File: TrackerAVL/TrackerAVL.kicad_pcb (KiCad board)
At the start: 2 copper layers, 120 x 80 mm, 173 parts, among them J801 Conn_02x07_Odd_Even, J802 Conn_01x15, J803 Conn_01x04, P201 uC_debug, Q201 DTC043ZEBTL, Q202 DTC043ZEBTL, Q203 DTC043ZEBTL, Q701 2N7002P, Q702 2N7002P, Q703 2N7002P, Q704 DTC043ZEBTL, U201 MAX3221, U202 LPC4337JBD144, U203 STS8C5H30L, U301 MPU-6050, U401 NAU8814, U501 STS8C5H30L, U502 LD1085D2T33R, U503 NCP114ASN180T1G, U601 MPCIE-Socket, U701 74LVC244APW, U801 74HC4053, X201 12MHz, X202 32.768K

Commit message: Cambios en pcb
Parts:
- moved JP203 3.41 mm to (210.4, 131.7)
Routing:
- net +3V3: track 450.8 -> 592.7 mm, vias 63 -> 76
- net /CPU/U2_RXD: track 0.00 -> 135.5 mm, vias 0 -> 4
- net /CPU/U2_TXD: track 0.00 -> 134.4 mm, vias 0 -> 4
- net /MIC+: track 22.7 -> 139.7 mm, vias 0 -> 4
- net /MIC-: track 17.8 -> 128.3 mm, vias 0 -> 4
- net GNDS: track 41.8 -> 144.7 mm, vias 3 -> 7
- net /CPU/SLEEP_MDM: track 0.00 -> 97.7 mm, vias 0 -> 2
- net /CPU/DIG_OUT_0: track 6.49 -> 87.4 mm, vias 0 -> 4
- net /CPU/IGN: track 0.00 -> 79.5 mm, vias 0 -> 12
- net /CPU/DIG_OUT_1: track 9.93 -> 85.5 mm, vias 0 -> 4
- net /CPU/U3_RX: track 37.3 -> 111.3 mm, vias 4 -> 2
- net /VBAT: track 32.4 -> 102.5 mm, vias 0 -> 6
- net /CPU/DIG_OUT_2: track 13.5 -> 83.7 mm, vias 0 -> 4
- net /CPU/U3_TX: track 39.0 -> 107.9 mm
- net /CPU/BUZZER: track 19.1 -> 84.2 mm, vias 0 -> 6
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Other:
- net class Default: clearance 0.25 -> 0.2
- rule trace_clearance: 0.25 -> 0.2

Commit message: PCB terminado, pendiente revisión
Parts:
- moved F103 83.0 mm to (124.0, 60.8)
- moved F104 75.8 mm to (206.5, 133.2)
- moved FB502 13.1 mm to (163.9, 115.8)
- moved R501 13.1 mm to (134.9, 124.7)
- moved U501 13.1 mm to (140.6, 123.8)
- moved C302 13.1 mm to (153.4, 59.6)
- moved C201 13.1 mm to (130.4, 126.2)
- moved C202 13.1 mm to (173.7, 99.1)
- moved C203 13.1 mm to (171.5, 99.1)
- moved C204 13.1 mm to (122.5, 133.0)
- moved C205 13.1 mm to (124.5, 133.0)
- moved C206 13.1 mm to (150.8, 72.9)
- moved C207 13.1 mm to (124.5, 129.0)
- moved C208 13.1 mm to (158.5, 76.8)
- moved C209 13.1 mm to (158.5, 79.3)
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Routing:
- net GNDS: track 144.7 -> 146.4 mm
- net GND: track 488.6 -> 487.1 mm
- net (no net): track 0.76 -> 0.00 mm
- added copper zone on B.Cu, net (none)
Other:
- board text added: "Equipo AVL vRaptor v1.0 STA"
- board text added: "Industria Argentina"
- board text added: "Referencia: Mayer (Tecnología 8 mils) Pistas: 1.5; 1; 0.75; 0.5; 0.25; 0.20 [mm] Vías: 0.8 - Agujero: 0.4 [mm] Márgen: 0.25 mm Pista más delgada: 0.2 mm Dist. a borde: 0.3 mm STACK-UP FR4 1.6 mm Dual layer Componentes en capa superior Máscara anti-soldante: Azul Sin requerimientos especiales Terminación: HASL c/Pb Espesor de Cu: 1oz"
- board text added: "[ 2]"
- board text added: "[1 ]"
- board text removed: "Equipo AVL vRaptor v1.0 Referencia: Mayer (Tecnología 8 mils) Pistas: 1,5; 1; 0,75; 0,5; 0,25 [mm] Vía: 1mm - Agujero: 0,5mm Márgen: 0,25mm Pista más delgada: 0,25mm Dist. a borde: 0,3mm STACK-UP FR4 1,6mm Dual layer Componentes en capa superior Máscara anti-soldante: Azul Sin requerimientos especiales Terminación: HASL c/Pb Espesor de Cu: 1oz"
- board text removed: "Recomendaciones diseño > Cruces de pista entre capas a 90° > Colocar buenos planos de masa > Considerar poner vías térmicas > Uniones entre pads y pistas "teardrop" > Para plano de masa, clearance 0.25mm mínimo > Colocar jumpers-open para medir consumos > Orientación silkscreen "para un mismo lado""

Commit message: PCB terminado, pendiente revisión
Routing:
- net +3V3: track 592.7 -> 620.1 mm, vias 76 -> 78
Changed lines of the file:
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@@
     (thickness 1.6)
     (drawings 32)
-    (tracks 2622)
+    (tracks 2634)
     (zones 0)
     (modules 173)
@@
   )
   (setup
-    (last_trace_width 0.5)
+    (last_trace_width 0.75)
     (user_trace_width 0.2)
     (user_trace_width 0.24)
@@
   (segment (start 125.95 68.95) (end 130.123008 73.123008) (width 0.5) (layer B.Cu) (net 2))
   (segment (start 138.45 80.5) (end 131.5 73.55) (width 0.5) (layer F.Cu) (net 2))
-  (segment (start 146.850001 107.350001) (end 163.950001 107.350001) (width 1.5) (layer F.Cu) (net 2))
   (segment (start 146 106.5) (end 146.850001 107.350001) (width 1.5) (layer F.Cu) (net 2))
   (segment (start 167.05 110.45) (end 204.15 110.45) (width 1.5) (layer F.Cu) (net 2))
@@
   (segment (start 132.917998 114.9) (end 125.617998 107.6) (width 0.5) (layer B.Cu) (net 2))
   (segment (start 124.15 106.15) (end 116.65 106.15) (width 0.5) (layer B.Cu) (net 2))
+  (segment (start 176.250001 96.549999) (end 176.250001 100.349999) (width 0.75) (layer F.Cu) (net 2))
+  (segment (start 176.35 96.5) (end 176.3 96.5) (width 0.75) (layer F.Cu) (net 2))
+  (segment (start 176.3 96.5) (end 176.250001 96.549999) (width 0.75) (layer F.Cu) (net 2))
+  (segment (start 176.250001 100.349999) (end 175.1 101.5) (width 0.75) (layer F.Cu) (net 2))
+  (via (at 168.1 101.5) (size 0.8) (drill 0.4) (layers F.Cu B.Cu) (net 2))
+  (segment (start 175.1 101.5) (end 168.1 101.5) (width 0.75) (layer F.Cu) (net 2))
+  (via (at 163.4 101.5) (size 0.8) (drill 0.4) (layers F.Cu B.Cu) (net 2))
+  (segment (start 168.1 101.5) (end 163.4 101.5) (width 0.75) (layer B.Cu) (net 2))
+  (segment (start 163.4 101.5) (end 161 101.5) (width 0.75) (layer F.Cu) (net 2))
+  (segment (start 161 101.5) (end 156.4 106.1) (width 0.75) (layer F.Cu) (net 2))
+  (segment (start 146.850001 107.350001) (end 156.4 107.350001) (width 1.5) (layer F.Cu) (net 2))
+  (segment (start 156.4 106.1) (end 156.4 107.350001) (width 0.75) (layer F.Cu) (net 2))
+  (segment (start 156.4 107.350001) (end 163.950001 107.350001) (width 1.5) (layer F.Cu) (net 2))
   (segment (start 173.60426 92.62074) (end 173.525 92.7) (width 0.24) (layer F.Cu) (net 3))
   (segment (start 173.60426 89.25182) (end 173.60426 92.62074) (width 0.24) (layer F.Cu) (net 3))
@@
     (polygon
       (pts
-        (xy 136.8 120.5) (xy 147 120.5) (xy 147 107.9) (xy 157.35 107.9) (xy 157.35 96)
+        (xy 136.8 120.5) (xy 147 120.5) (xy 147 107.9) (xy 162 107.95) (xy 162 96.05)
         (xy 137.25 96) (xy 136.8 96)
       )

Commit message: PCB terminado, pendiente revisión
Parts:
- moved C504 10.0 mm to (155.6, 120.5)
- moved D501 10.0 mm to (139.2, 118.0)
- moved F501 10.0 mm to (137.8, 121.8)
- moved C214 10.0 mm to (161.0, 60.8)
- moved C301 10.0 mm to (153.4, 55.1)
- moved C201 10.0 mm to (130.4, 116.2)
- moved C202 10.0 mm to (173.7, 89.1)
- moved C203 10.0 mm to (171.5, 89.1)
- moved C204 10.0 mm to (122.5, 123.0)
- moved C205 10.0 mm to (124.5, 123.0)
- moved C206 10.0 mm to (150.8, 62.9)
- moved C207 10.0 mm to (124.5, 119.0)
- moved C208 10.0 mm to (158.5, 66.8)
- moved C209 10.0 mm to (158.5, 69.3)
- moved C210 10.0 mm to (122.5, 119.0)
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
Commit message: vRaptor-v1.1-init
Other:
- board text added: "vRaptor v1.0 STA"
- board text removed: "Equipo AVL vRaptor v1.0 STA"
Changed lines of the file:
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@@
   )
   (setup
-    (last_trace_width 0.75)
+    (last_trace_width 0.25)
     (user_trace_width 0.2)
     (user_trace_width 0.24)
@@
     (arrow2b (pts (xy 111.5 147) (xy 112.626504 146.413579)))
   )
-  (gr_text "Equipo AVL \nvRaptor v1.0\nSTA" (at 123.5 52.5) (layer F.SilkS)
+  (gr_text "vRaptor v1.0\nSTA" (at 123.5 51) (layer F.SilkS)
     (effects (font (size 1.5 1.5) (thickness 0.3)) (justify left))
   )

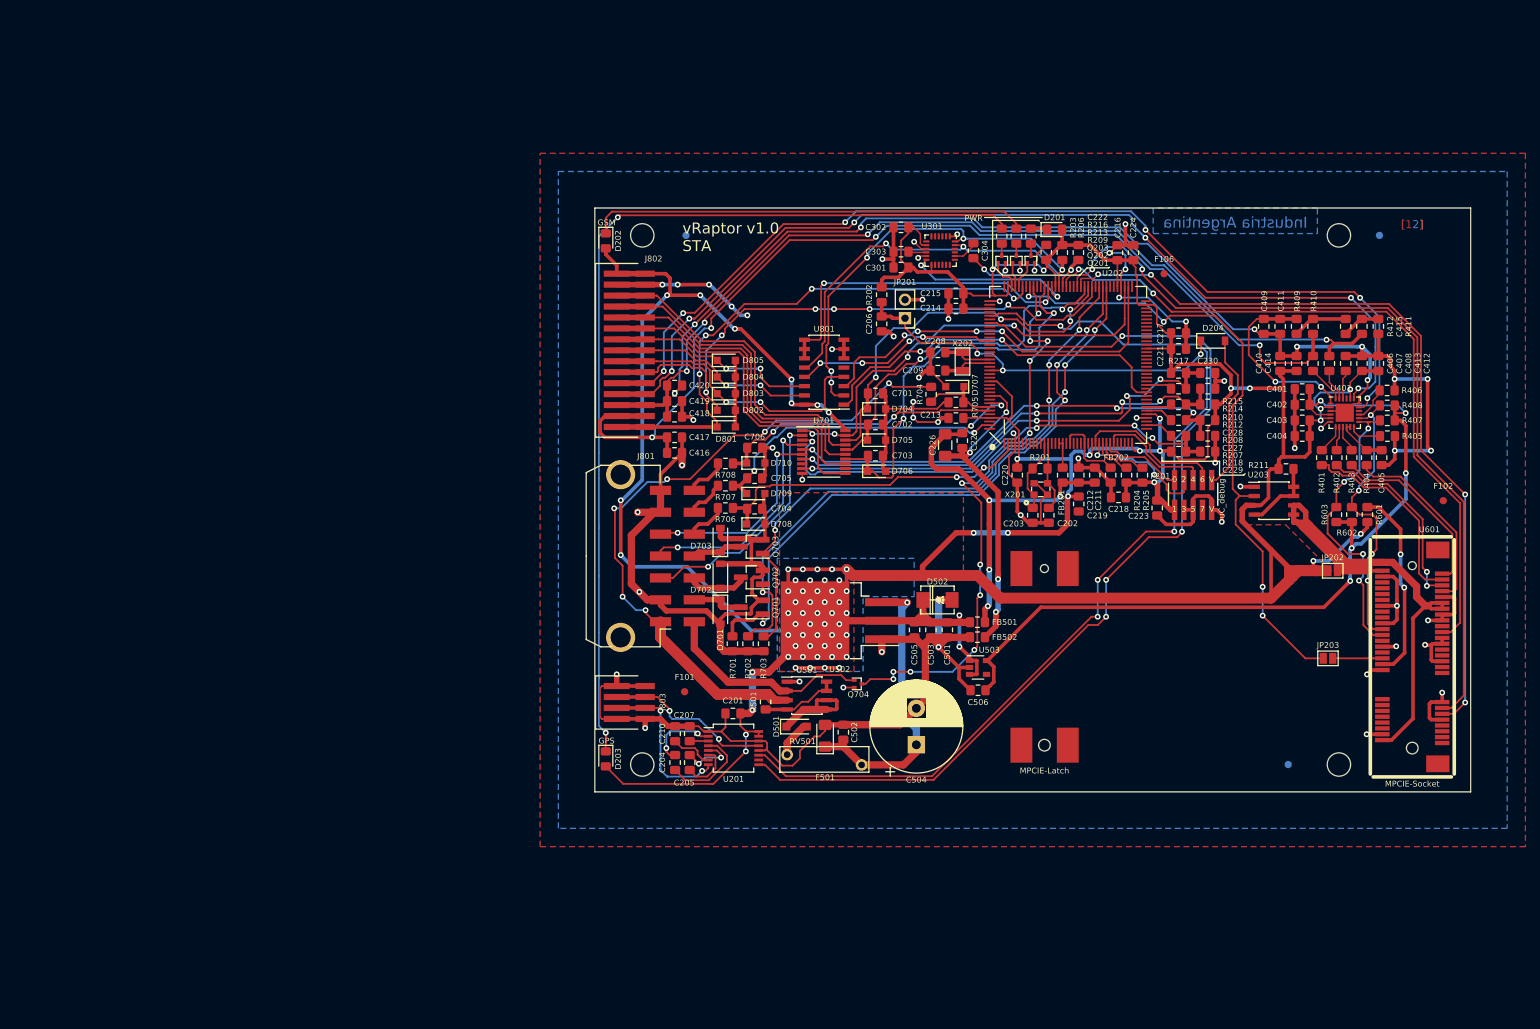
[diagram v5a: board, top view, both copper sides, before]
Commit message: Se modifica huella NAU8814 a QFN-24_HandSoldering
Falta modificar resto de huellas
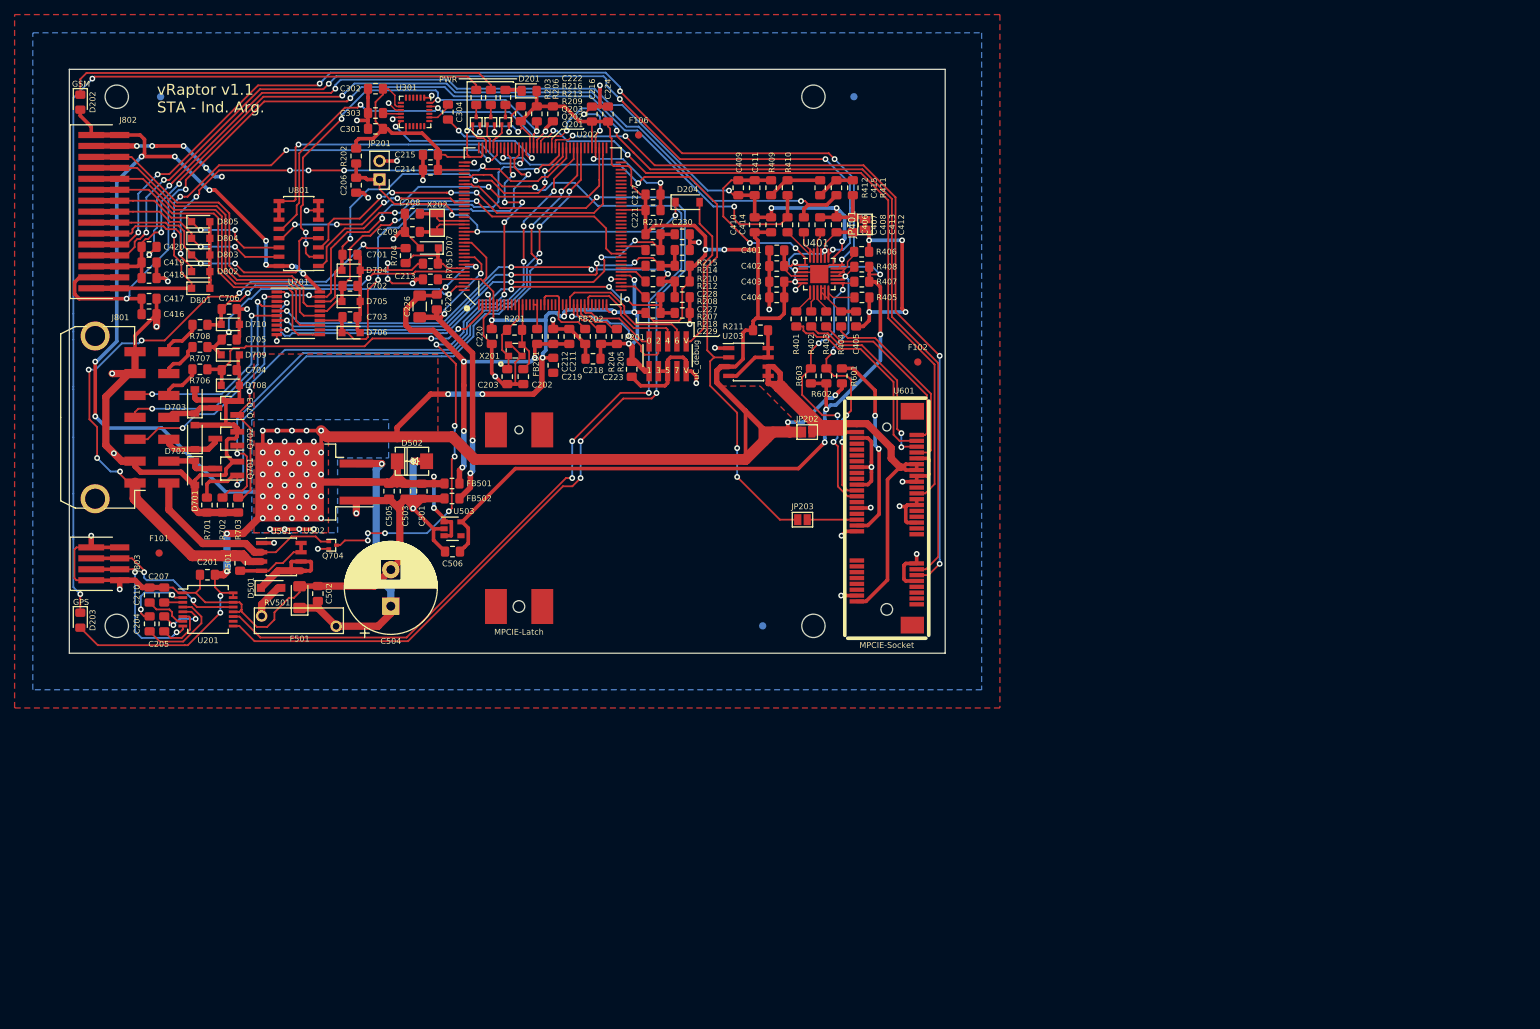
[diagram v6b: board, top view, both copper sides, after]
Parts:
- JP401: footprint NetTie:NetTie-2_SMD_Pad0.5mm -> Jumper:SolderJumper-2_P1.3mm_Bridged_Pad1.0x1.5mm
- U401: footprint nau8814:NAU8814_QFN-24_4x4mm_Pitch0.5mm_EPAD -> nau8814:NAU8814_QFN-24_4x4mm_Pitch0.5mm_EPAD_HandSoldering
- moved C201 74.5 mm to (58.4, 97.2)
- moved C206 74.5 mm to (78.8, 43.9)
- moved C208 74.5 mm to (86.5, 47.8)
- moved C209 74.5 mm to (86.5, 50.3)
- moved C212 74.5 mm to (105.8, 64.6)
- moved C213 74.5 mm to (89.0, 56.8)
- moved C219 74.5 mm to (105.8, 68.5)
- moved C221 74.5 mm to (119.5, 45.1)
- moved C223 74.5 mm to (116.5, 69.1)
- moved C224 74.5 mm to (113.3, 34.1)
- moved C419 74.5 mm to (50.4, 54.5)
- moved C501 74.5 mm to (87.8, 85.8)
- moved C502 74.5 mm to (73.5, 99.8)
- moved C503 74.5 mm to (85.5, 85.8)
- moved C504 74.5 mm to (83.5, 101.5)
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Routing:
- removed copper zone on B.Cu, net (none)
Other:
- board text added: "A modificar en v1.1: > Pistas que acceden a pads, que sea a 90°, y lo más estranguladas posibles (grosor pista << grosor pad). > Pistas que entren/salen de un mismo componente, que sean homogeneas (mismo ancho). > Pads QFN alargarlos, para facilitar el soldado. El ta- maño del pad aprox. 1.5mm (ese es el ancho de la superficie del pad que la punta del soldador debe hacer contacto -punta 900m-t-2c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"
- board text added: "vRaptor v1.1 STA - Ind. Arg."
- board text removed: "Industria Argentina"
- board text removed: "[ 2]"
- board text removed: "[1 ]"
- board text removed: "vRaptor v1.0 STA"

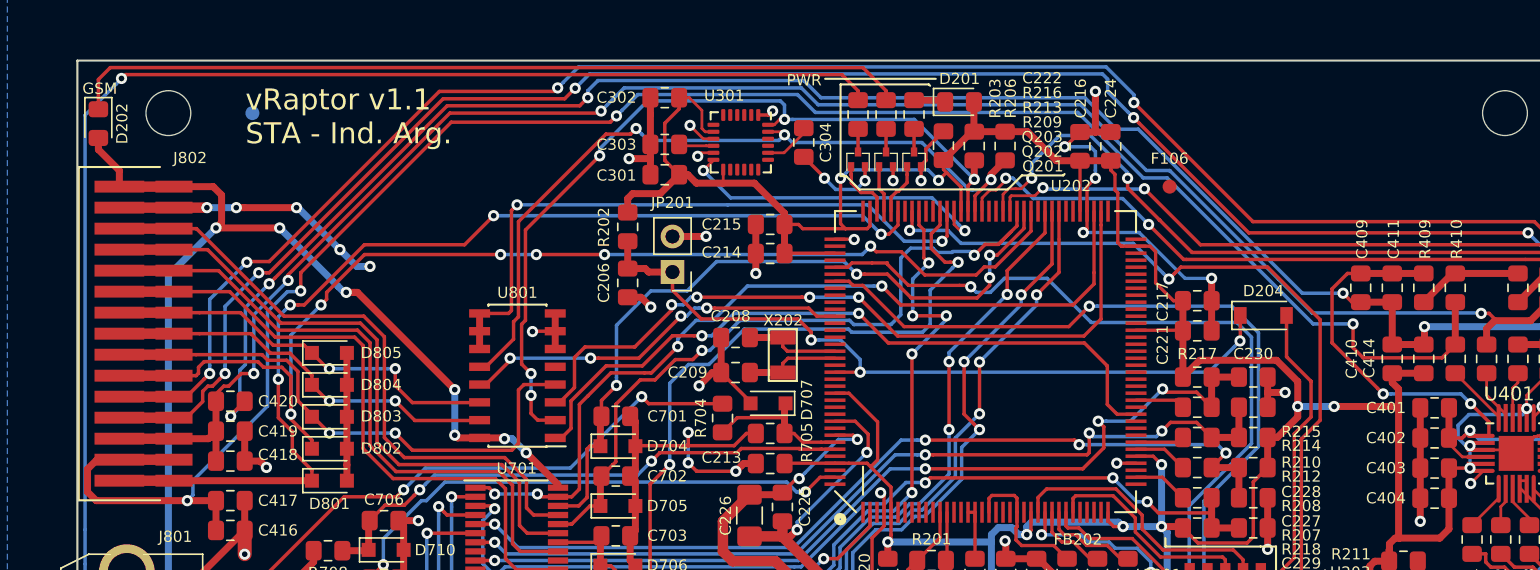
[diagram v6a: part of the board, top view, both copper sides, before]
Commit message: Se modifica huella MPU6050 a QFN-24_HandSoldering
Pendiente hacer cambios de pistas según recomendaciones que figuran en el diseño del pcb.
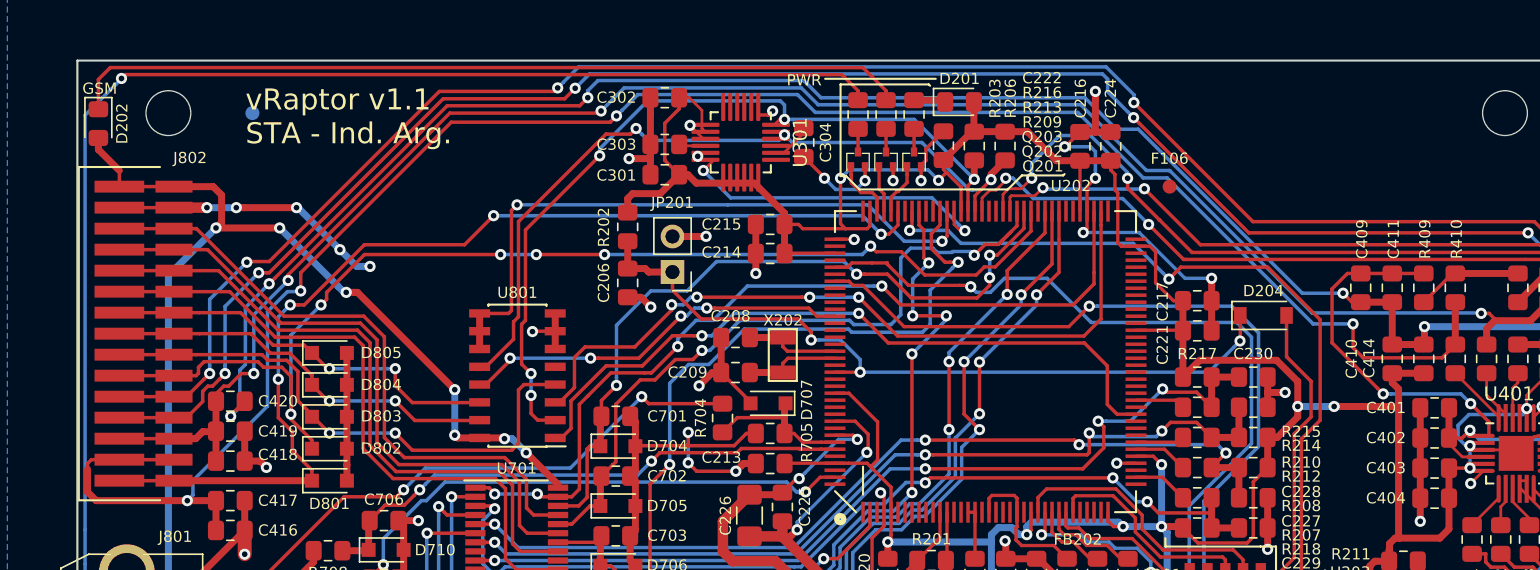
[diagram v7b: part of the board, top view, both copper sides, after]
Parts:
- U301: footprint Sensor_Motion:InvenSense_QFN-24_4x4mm_P0.5mm -> Sensor_Motion:InvenSense_QFN-24_4x4mm_P0.5mm_HandSoldering
